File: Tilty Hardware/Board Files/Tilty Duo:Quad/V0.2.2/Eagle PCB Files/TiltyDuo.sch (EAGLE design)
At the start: 38 parts, among them U1 TEENSY_3.0_OUTER-PINS28-DIP_S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, U2 HC-09_BREAKOUT, U3 MPL3115A2LGA8, U4 LM2931, U5 MPU-6050, U6 HMC5883LSMD

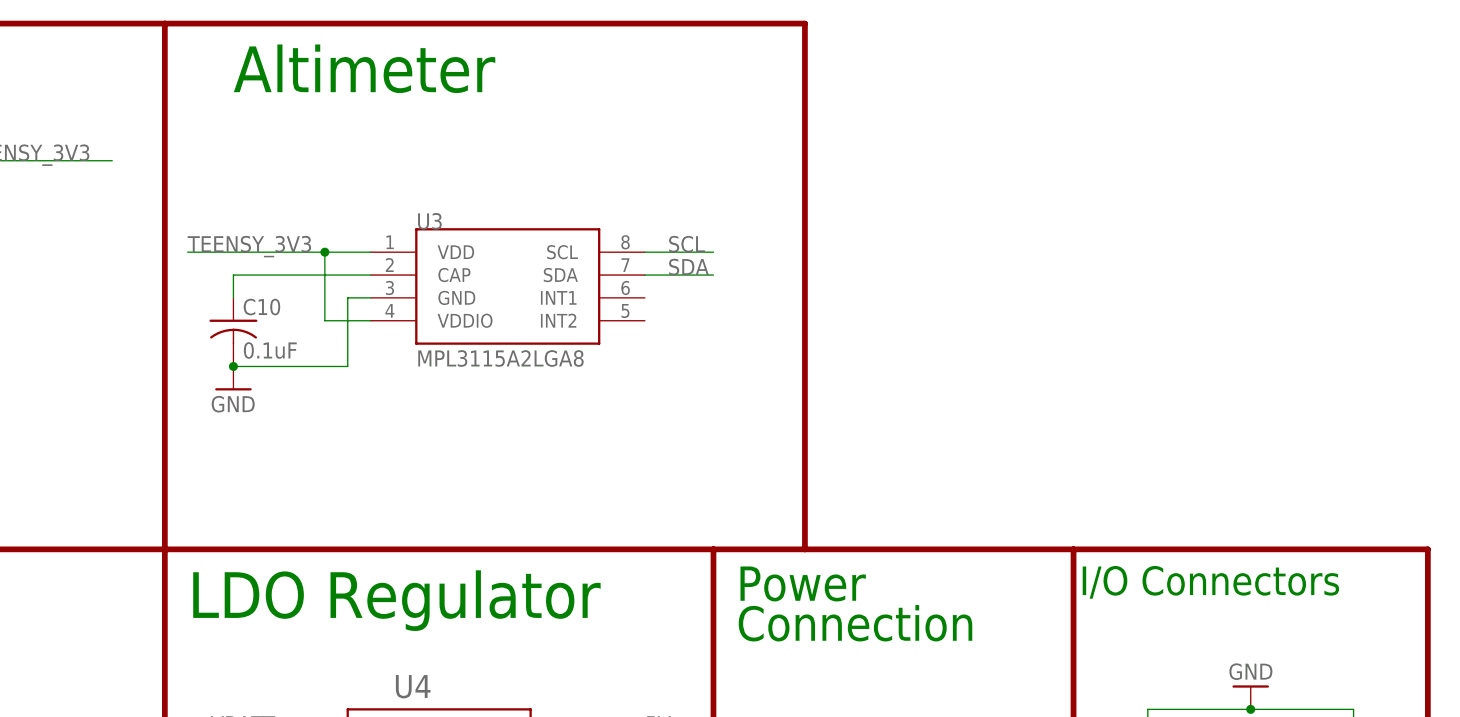
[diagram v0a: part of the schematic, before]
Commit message: Added 1kB EEPROM chip to V0.2.2 board
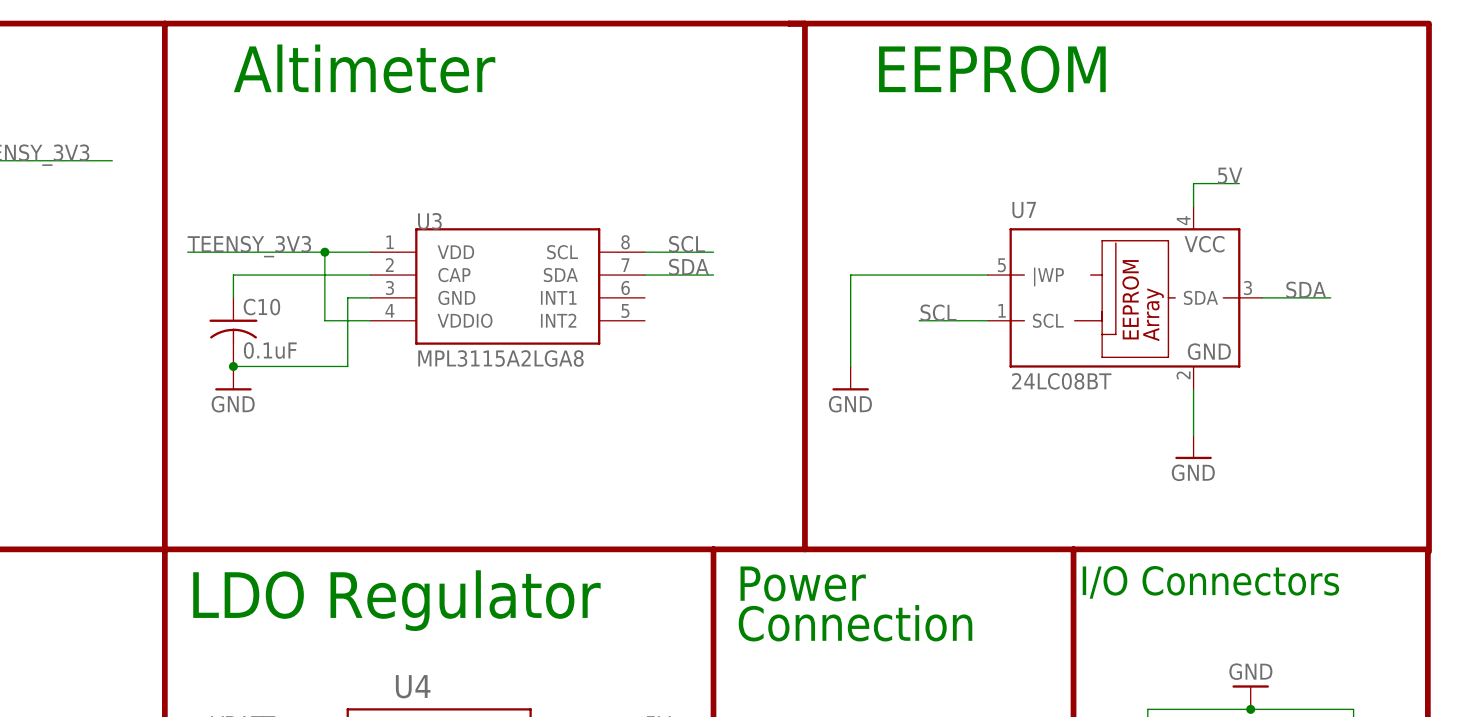
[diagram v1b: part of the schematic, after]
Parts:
- added U7: 24LC08BT, microchip:24LC08BT
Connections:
- net 5V: now also U7.VCC
- net GND: now also U7.GND, U7.|WP
- net SCL: now also U7.SCL
- net SDA: now also U7.SDA
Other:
- note added: "EEPROM"
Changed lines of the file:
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@@
 <grid distance="0.1" unitdist="inch" unit="inch" style="lines" multiple="1" display="no" altdistance="0.01" altunitdist="inch" altunit="inch"/>
 <layers>
-<layer number="1" name="Top" color="4" fill="1" visible="yes" active="no"/>
-<layer number="16" name="Bottom" color="1" fill="1" visible="yes" active="no"/>
-<layer number="17" name="Pads" color="2" fill="1" visible="yes" active="no"/>
-<layer number="18" name="Vias" color="2" fill="1" visible="yes" active="no"/>
-<layer number="19" name="Unrouted" color="6" fill="1" visible="yes" active="no"/>
-<layer number="20" name="Dimension" color="15" fill="1" visible="yes" active="no"/>
-<layer number="21" name="tPlace" color="7" fill="1" visible="yes" active="no"/>
-<layer number="22" name="bPlace" color="7" fill="1" visible="yes" active="no"/>
-<layer number="23" name="tOrigins" color="15" fill="1" visible="yes" active="no"/>
-<layer number="24" name="bOrigins" color="15" fill="1" visible="yes" active="no"/>
-<layer number="25" name="tNames" color="14" fill="1" visible="yes" active="no"/>
-<layer number="26" name="bNames" color="6" fill="1" visible="yes" active="no"/>
-<layer number="27" name="tValues" color="7" fill="1" visible="yes" active="no"/>
-<layer number="28" name="bValues" color="7" fill="1" visible="yes" active="no"/>
+<layer number="1" name="Top" color="4" fill="1" visible="no" active="no"/>
+<layer number="16" name="Bottom" color="1" fill="1" visible="no" active="no"/>
+<layer number="17" name="Pads" color="2" fill="1" visible="no" active="no"/>
+<layer number="18" name="Vias" color="2" fill="1" visible="no" active="no"/>
+<layer number="19" name="Unrouted" color="6" fill="1" visible="no" active="no"/>
+<layer number="20" name="Dimension" color="15" fill="1" visible="no" active="no"/>
+<layer number="21" name="tPlace" color="7" fill="1" visible="no" active="no"/>
+<layer number="22" name="bPlace" color="7" fill="1" visible="no" active="no"/>
+<layer number="23" name="tOrigins" color="15" fill="1" visible="no" active="no"/>
+<layer number="24" name="bOrigins" color="15" fill="1" visible="no" active="no"/>
+<layer number="25" name="tNames" color="14" fill="1" visible="no" active="no"/>
+<layer number="26" name="bNames" color="6" fill="1" visible="no" active="no"/>
+<layer number="27" name="tValues" color="7" fill="1" visible="no" active="no"/>
+<layer number="28" name="bValues" color="7" fill="1" visible="no" active="no"/>
 <layer number="29" name="tStop" color="7" fill="3" visible="no" active="no"/>
 <layer number="30" name="bStop" color="7" fill="6" visible="no" active="no"/>
@@
 <layer number="35" name="tGlue" color="7" fill="4" visible="no" active="no"/>
 <layer number="36" name="bGlue" color="7" fill="5" visible="no" active="no"/>
-<layer number="37" name="tTest" color="7" fill="1" visible="yes" active="no"/>
-<layer number="38" name="bTest" color="7" fill="1" visible="yes" active="no"/>
+<layer number="37" name="tTest" color="7" fill="1" visible="no" active="no"/>
+<layer number="38" name="bTest" color="7" fill="1" visible="no" active="no"/>
 <layer number="39" name="tKeepout" color="4" fill="11" visible="no" active="no"/>
 <layer number="40" name="bKeepout" color="1" fill="11" visible="no" active="no"/>
@@
 <layer number="44" name="Drills" color="7" fill="1" visible="no" active="no"/>
 <layer number="45" name="Holes" color="7" fill="1" visible="no" active="no"/>
-<layer number="46" name="Milling" color="3" fill="1" visible="yes" active="no"/>
-<layer number="47" name="Measures" color="7" fill="1" visible="yes" active="no"/>
-<layer number="48" name="Document" color="7" fill="1" visible="yes" active="no"/>
-<layer number="49" name="Reference" color="7" fill="1" visible="yes" active="no"/>
-<layer number="50" name="dxf" color="7" fill="1" visible="yes" active="no"/>
-<layer number="51" name="tDocu" color="7" fill="1" visible="yes" active="no"/>
-<layer number="52" name="bDocu" color="7" fill="1" visible="yes" active="no"/>
-<layer number="53" name="tGND_GNDA" color="7" fill="9" visible="yes" active="no"/>
-<layer number="54" name="bGND_GNDA" color="1" fill="9" visible="yes" active="no"/>
-<layer number="56" name="wert" color="7" fill="1" visible="yes" active="no"/>
+<layer number="46" name="Milling" color="3" fill="1" visible="no" active="no"/>
+<layer number="47" name="Measures" color="7" fill="1" visible="no" active="no"/>
+<layer number="48" name="Document" color="7" fill="1" visible="no" active="no"/>
+<layer number="49" name="Reference" color="7" fill="1" visible="no" active="no"/>
+<layer number="50" name="dxf" color="7" fill="1" visible="no" active="no"/>
+<layer number="51" name="tDocu" color="7" fill="1" visible="no" active="no"/>
+<layer number="52" name="bDocu" color="7" fill="1" visible="no" active="no"/>
+<layer number="53" name="tGND_GNDA" color="7" fill="9" visible="no" active="no"/>
+<layer number="54" name="bGND_GNDA" color="1" fill="9" visible="no" active="no"/>
+<layer number="56" name="wert" color="7" fill="1" visible="no" active="no"/>
 <layer number="91" name="Nets" color="2" fill="1" visible="yes" active="yes"/>
 <layer number="92" name="Busses" color="1" fill="1" visible="yes" active="yes"/>
@@
 <part name="GND7" library="supply1" deviceset="GND" device=""/>
 <part name="R8" library="resistor" deviceset="R-US_" device="R0603" value="68"/>
+<part name="U7" library="microchip" deviceset="24LC08BT" device=""/>
+<part name="GND22" library="SparkFun" deviceset="GND" device=""/>
+<part name="GND23" library="SparkFun" deviceset="GND" device=""/>
 </parts>
 <sheets>
@@
 <text x="12.7" y="184.15" size="6.35" layer="91" ratio="14">Compass Circuitry</text>
 <wire x1="182.88" y1="193.04" x2="182.88" y2="134.62" width="0.635" layer="94"/>
-<wire x1="111.76" y1="193.04" x2="182.88" y2="193.04" width="0.635" layer="94"/>
+<wire x1="111.76" y1="193.04" x2="181.102" y2="193.04" width="0.635" layer="94"/>
 <text x="119.38" y="185.42" size="5.08" layer="91" ratio="14">Altimeter</text>
+<wire x1="181.102" y1="193.04" x2="182.88" y2="193.04" width="0.635" layer="94"/>
+<wire x1="252.222" y1="192.786" x2="252.222" y2="134.366" width="0.635" layer="94"/>
+<wire x1="181.102" y1="193.04" x2="252.222" y2="193.04" width="0.635" layer="94"/>
+<text x="190.5" y="185.42" size="5.08" layer="91" ratio="14">EEPROM</text>
 </plain>
 <instances>
@@
 <instance part="GND7" gate="1" x="73.914" y="24.384"/>
 <instance part="R8" gate="G$1" x="73.914" y="32.004" rot="R90"/>
+<instance part="U7" gate="G$1" x="218.44" y="162.56"/>
+<instance part="GND22" gate="1" x="187.96" y="152.4"/>
+<instance part="GND23" gate="1" x="226.06" y="144.78"/>
 </instances>
 <busses>
@@
 <pinref part="R8" gate="G$1" pin="1"/>
 </segment>
+<segment>
+<pinref part="U7" gate="G$1" pin="|WP"/>
+<wire x1="203.2" y1="165.1" x2="187.96" y2="165.1" width="0.1524" layer="91"/>
+<wire x1="187.96" y1="165.1" x2="187.96" y2="154.94" width="0.1524" layer="91"/>
+<pinref part="GND22" gate="1" pin="GND"/>
+</segment>
+<segment>
+<pinref part="U7" gate="G$1" pin="GND"/>
+<wire x1="226.06" y1="152.4" x2="226.06" y2="147.32" width="0.1524" layer="91"/>
+<pinref part="GND23" gate="1" pin="GND"/>
+</segment>
 </net>
 <net name="SCL" class="4">
@@
 <label x="167.64" y="167.64" size="1.778" layer="95"/>
 </segment>
+<segment>
+<pinref part="U7" gate="G$1" pin="SCL"/>
+<wire x1="203.2" y1="160.02" x2="195.58" y2="160.02" width="0.1524" layer="91"/>
+<label x="195.58" y="160.02" size="1.778" layer="95"/>
+</segment>
 </net>
 <net name="SDA" class="4">
@@
 <wire x1="165.1" y1="165.1" x2="172.72" y2="165.1" width="0.1524" layer="91"/>
 <label x="167.64" y="165.1" size="1.778" layer="95"/>
+</segment>
+<segment>
+<pinref part="U7" gate="G$1" pin="SDA"/>
+<wire x1="233.68" y1="162.56" x2="241.3" y2="162.56" width="0.1524" layer="91"/>
+<label x="236.22" y="162.56" size="1.778" layer="95"/>
 </segment>
 </net>
@@
 <label x="76.454" y="72.644" size="1.778" layer="95"/>
 </segment>
-</net>
+<segment>
+<pinref part="U7" gate="G$1" pin="VCC"/>
+<wire x1="226.06" y1="172.72" x2="226.06" y2="175.26" width="0.1524" layer="91"/>
+<wire x1="226.06" y1="175.26" x2="231.14" y2="175.26" width="0.1524" layer="91"/>
+<label x="228.6" y="175.26" size="1.778" layer="95"/>
+</segment>
+</net>
